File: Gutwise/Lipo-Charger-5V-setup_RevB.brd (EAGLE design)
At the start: 66 x 45 mm, 10 parts

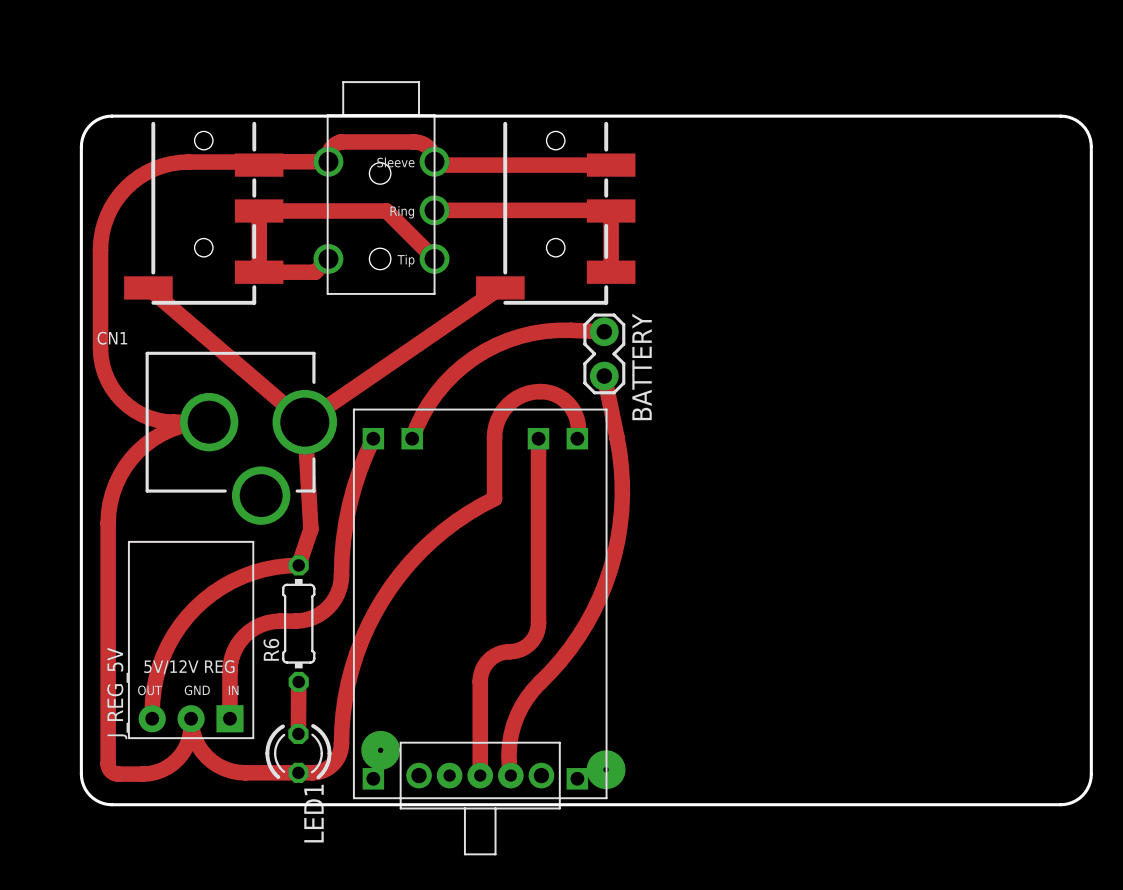
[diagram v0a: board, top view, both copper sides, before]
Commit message: new Gutwise power board
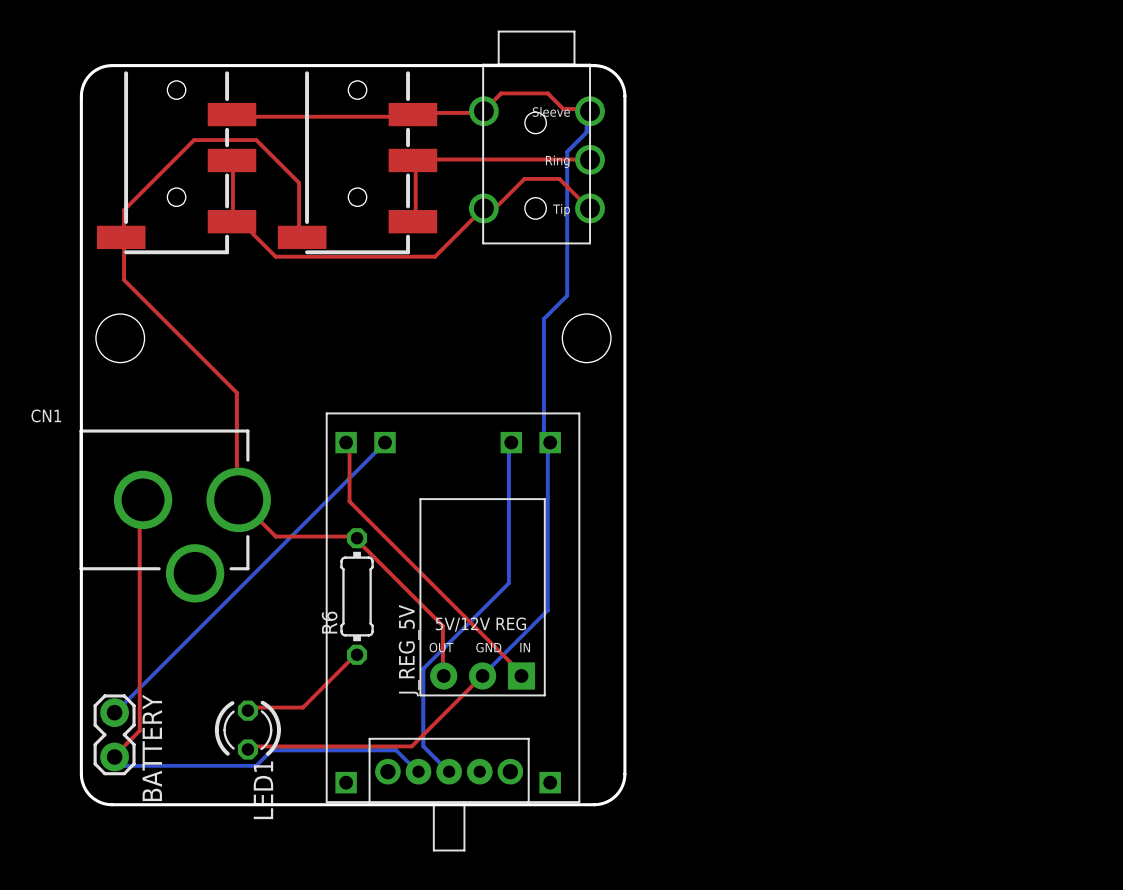
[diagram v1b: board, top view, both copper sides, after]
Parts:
- moved BATTERY 40.5 mm to (2.17, 5.84)
- moved J_REG_5V 19.3 mm to (26.2, 14.8)
- moved U$5 13.4 mm to (18.0, 48.3)
- moved AUDIO_OUT 10.7 mm to (33.2, 36.7)
- moved CN1 6.67 mm to (-3.32, 19.9)
- moved R6 4.20 mm to (18.0, 13.6)
- moved U$4 3.75 mm to (6.22, 48.3)
- moved LED1 3.64 mm to (10.9, 4.88)
- moved POWER 2.05 mm to (20.0, 2.16)
- moved USB-LIPO-CHARGER 1.80 mm to (24.3, 12.9)
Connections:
- net GND: no longer CN1.GND
- net N$1: now also CN1.GND, POWER.1; no longer POWER.3
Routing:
- net GND: track 128.5 -> 82.2 mm
- net N$1: track 27.3 -> 38.7 mm
- net N$18: track 14.7 -> 25.0 mm
- net OUT2: track 21.6 -> 31.3 mm
- net +5V: track 52.5 -> 60.6 mm
- net N$2: track 3.40 -> 8.71 mm
- net VIN: track 22.1 -> 20.1 mm
- net N$19: track 23.6 -> 24.6 mm
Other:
- board size 66 x 45 mm -> 35.5 x 48.3 mm

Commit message: new Gutwise power board
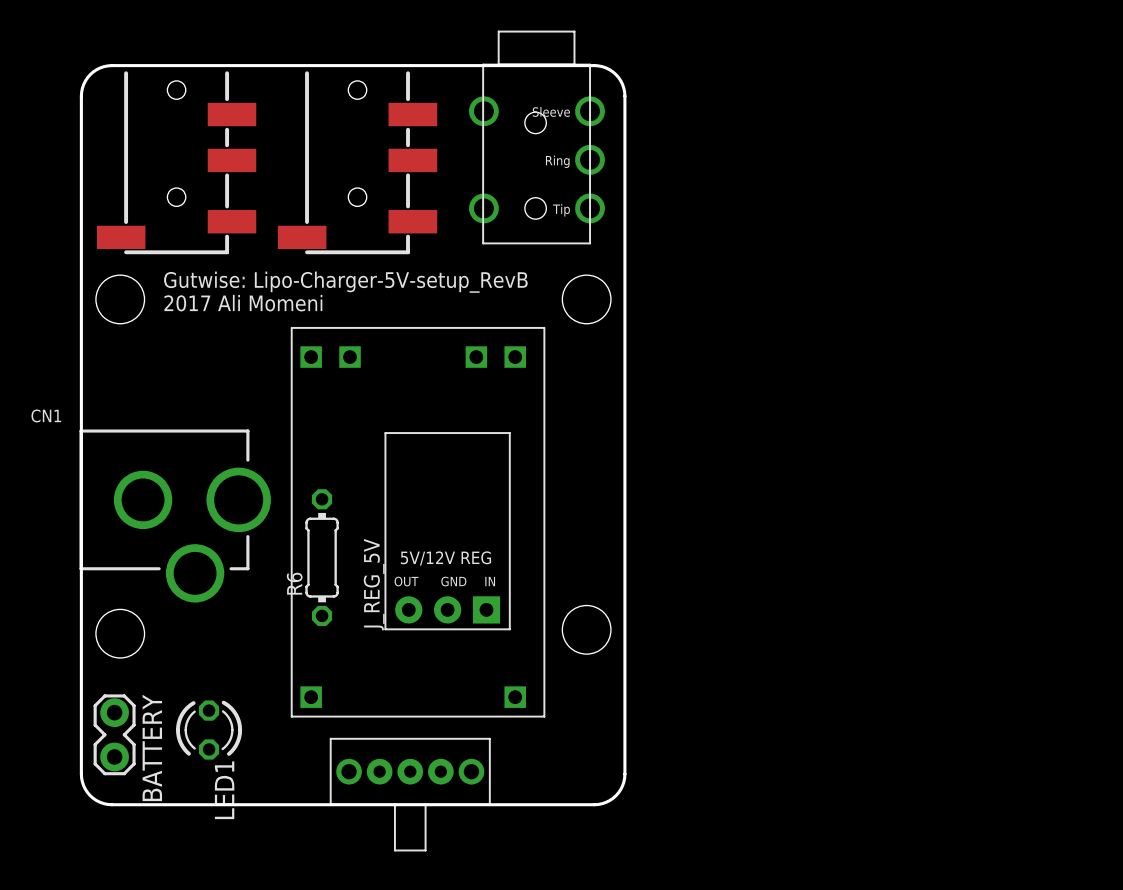
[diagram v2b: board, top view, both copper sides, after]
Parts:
- moved USB-LIPO-CHARGER 6.04 mm to (22.0, 18.5)
- moved J_REG_5V 4.89 mm to (23.9, 19.1)
- moved R6 3.42 mm to (15.7, 16.1)
- moved POWER 2.54 mm to (17.5, 2.16)
- moved LED1 2.54 mm to (8.34, 4.88)
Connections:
- removed net N$19: POWER.2, USB-LIPO-CHARGER.B-
- new net N$3: POWER.3, USB-LIPO-CHARGER.B-
- net N$1: now also POWER.2; no longer POWER.1
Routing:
- net GND: track 82.2 -> 0.00 mm
- net +5V: track 60.6 -> 0.00 mm
- net N$1: track 38.7 -> 0.00 mm
- net OUT2: track 31.3 -> 0.00 mm
- net N$18: track 25.0 -> 0.00 mm
- net N$19: track 24.6 -> 0.00 mm
- net VIN: track 20.1 -> 0.00 mm
- net N$8: track 15.7 -> 0.00 mm
- net N$2: track 8.71 -> 0.00 mm
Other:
- board text added: "2017 Ali Momeni"
- board text added: "Gutwise: Lipo-Charger-5V-setup_RevB"

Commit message: new Gutwise power board
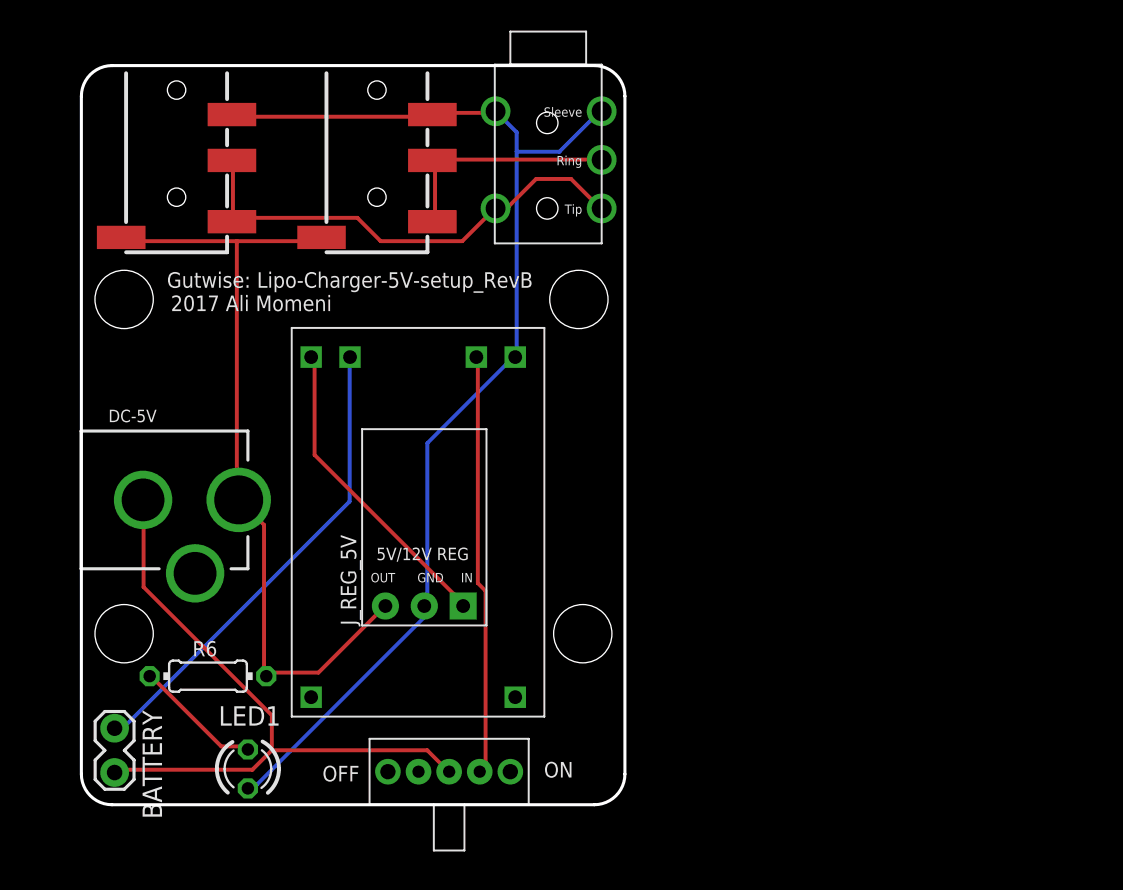
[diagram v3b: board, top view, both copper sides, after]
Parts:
- moved R6 10.8 mm to (8.27, 8.40), turned to 0 degrees
- moved LED1 3.59 mm to (10.9, 2.34)
- moved POWER 2.54 mm to (20.0, 2.16)
- moved J_REG_5V 1.55 mm to (22.4, 19.3)
- moved U$5 1.27 mm to (19.3, 48.3)
- moved BATTERY 1.02 mm to (2.17, 4.82)
- moved AUDIO_OUT 0.76 mm to (34.0, 36.7)
- renumbered CN1 to DC-5V
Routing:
- net GND: track 0.00 -> 76.5 mm
- net +5V: track 0.00 -> 52.3 mm
- net N$1: track 0.00 -> 42.9 mm
- net OUT2: track 0.00 -> 31.2 mm
- net N$18: track 0.00 -> 30.9 mm
- net N$3: track 0.00 -> 27.5 mm
- net VIN: track 0.00 -> 20.5 mm
- net N$8: track 0.00 -> 15.2 mm
- net N$2: track 0.00 -> 8.39 mm
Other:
- board text added: "OFF"
- board text added: "ON"
